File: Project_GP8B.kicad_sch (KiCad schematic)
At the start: 19 parts

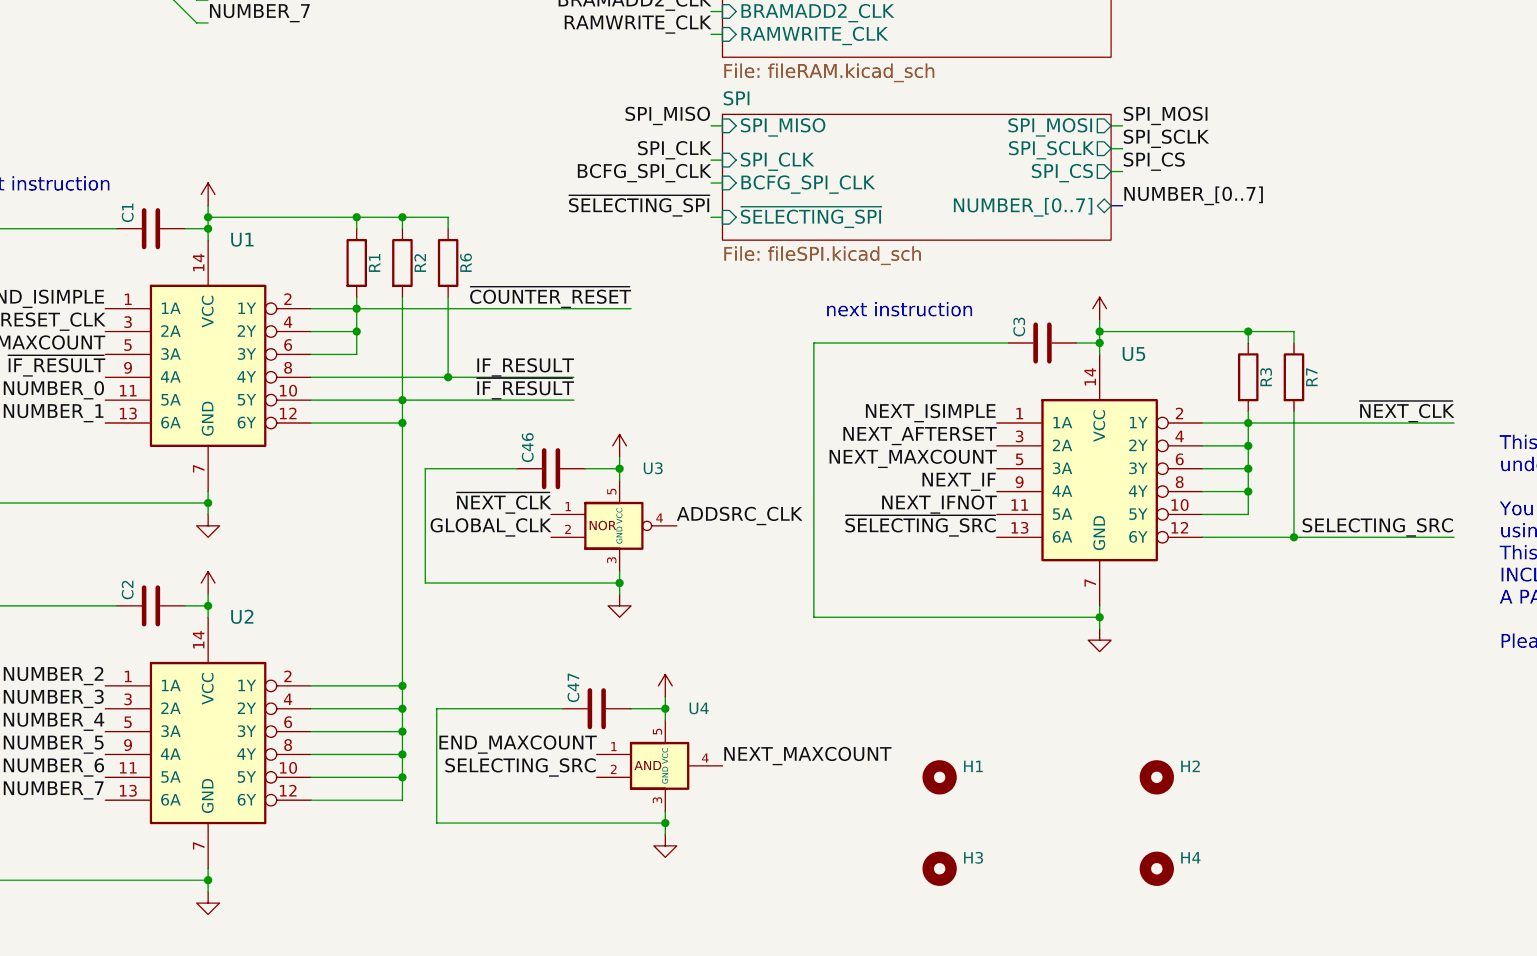
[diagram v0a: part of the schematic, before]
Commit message: Updating descriptions
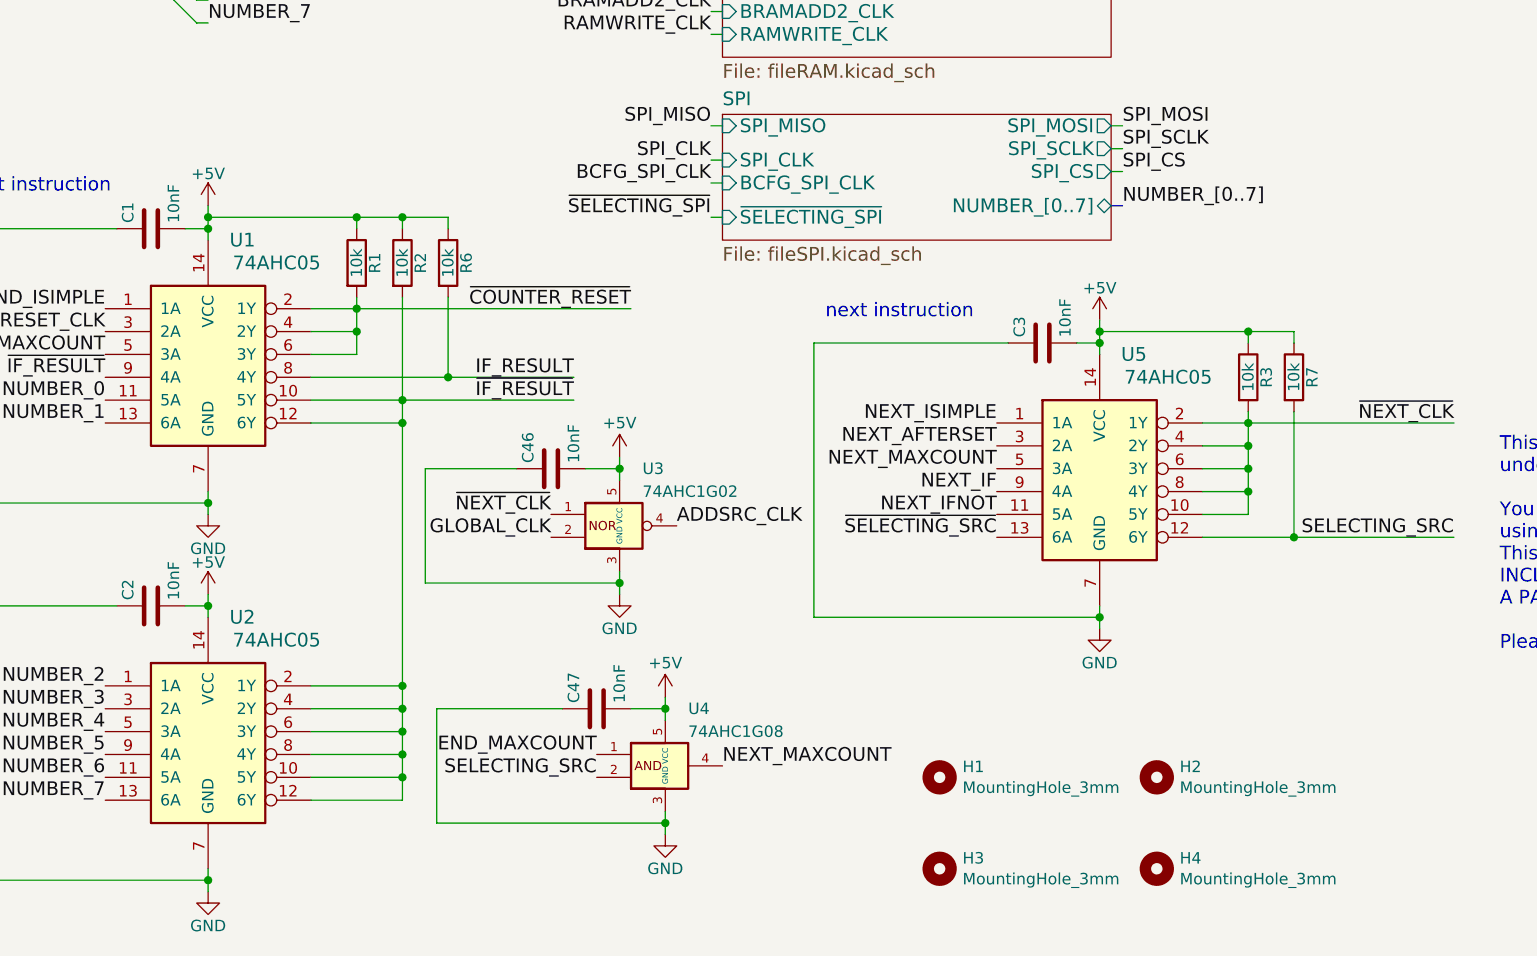
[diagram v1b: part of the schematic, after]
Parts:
- C1, C2, C3, C46, C47: value (none) -> 10nF; footprint (none) -> Capacitor_SMD:C_0805_2012Metric
- H1, H2, H3, H4: value (none) -> MountingHole_3mm; footprint (none) -> MountingHole:MountingHole_3mm
- R1, R2, R3, R6, R7: value (none) -> 10k; footprint (none) -> Resistor_SMD:R_0805_2012Metric
- U1, U2, U5: value (none) -> 74AHC05; footprint (none) -> Package_SO:SOIC-14_3.9x8.7mm_P1.27mm
- U3: value (none) -> 74AHC1G02; footprint (none) -> Package_TO_SOT_SMD:SOT-23-5
- U4: value (none) -> 74AHC1G08; footprint (none) -> Package_TO_SOT_SMD:SOT-23-5

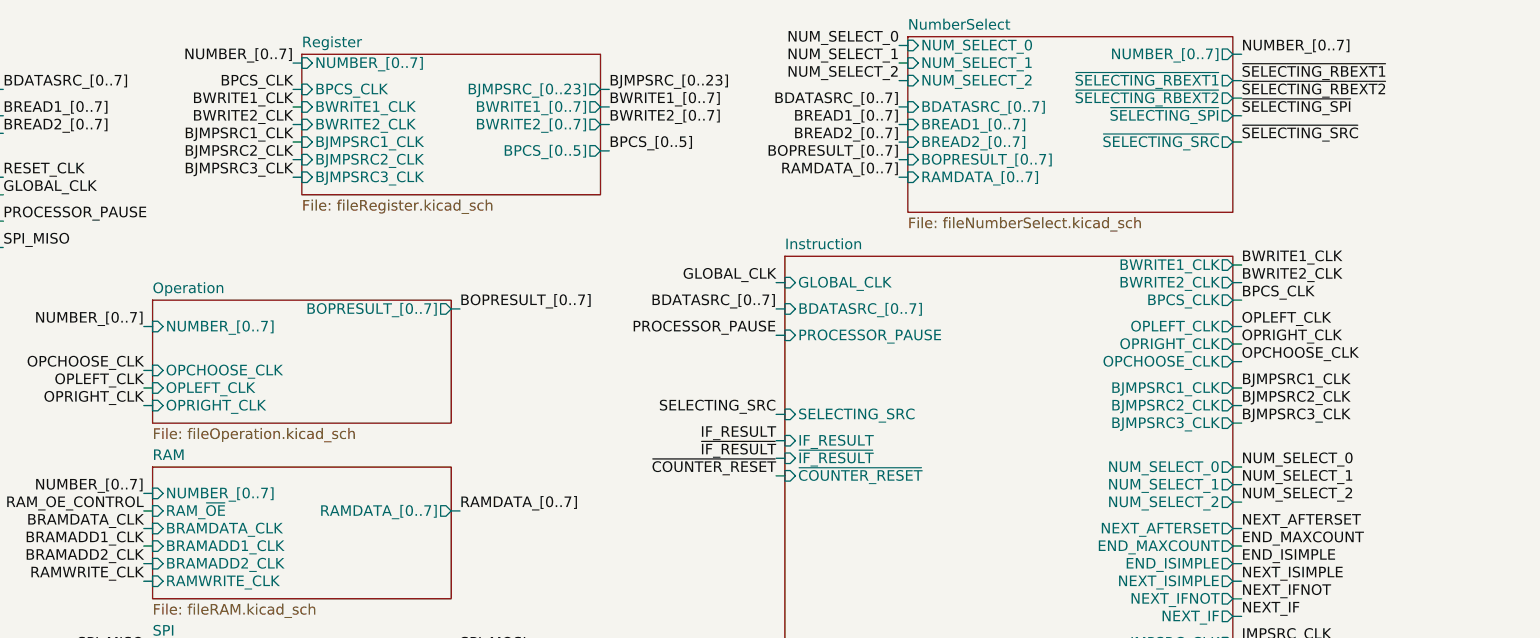
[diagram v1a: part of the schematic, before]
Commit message: Renaming COUNTER to SEQUENCE and others to make it clear
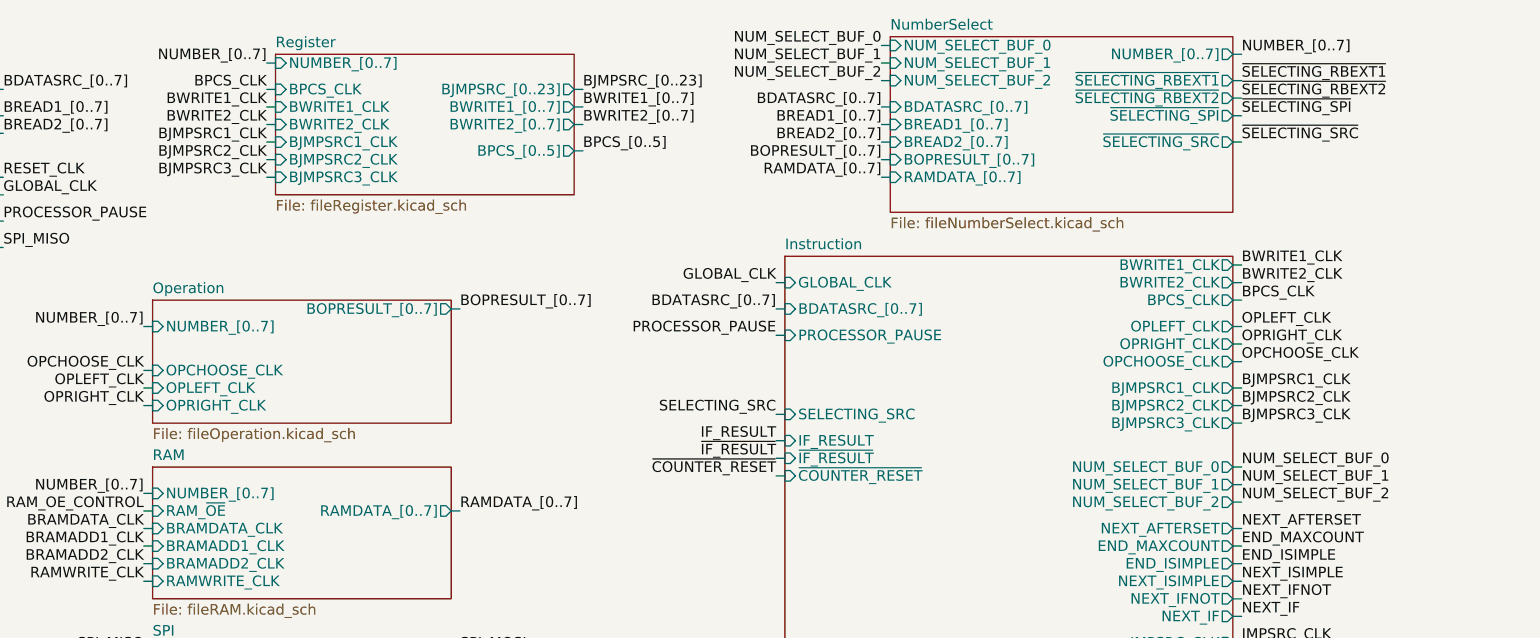
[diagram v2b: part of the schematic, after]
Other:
- sheet Instruction ports: added NUM_SELECT_BUF_0, NUM_SELECT_BUF_1, NUM_SELECT_BUF_2; removed NUM_SELECT_0, NUM_SELECT_1, NUM_SELECT_2
- sheet NumberSelect ports: added NUM_SELECT_BUF_0, NUM_SELECT_BUF_1, NUM_SELECT_BUF_2; removed NUM_SELECT_0, NUM_SELECT_1, NUM_SELECT_2

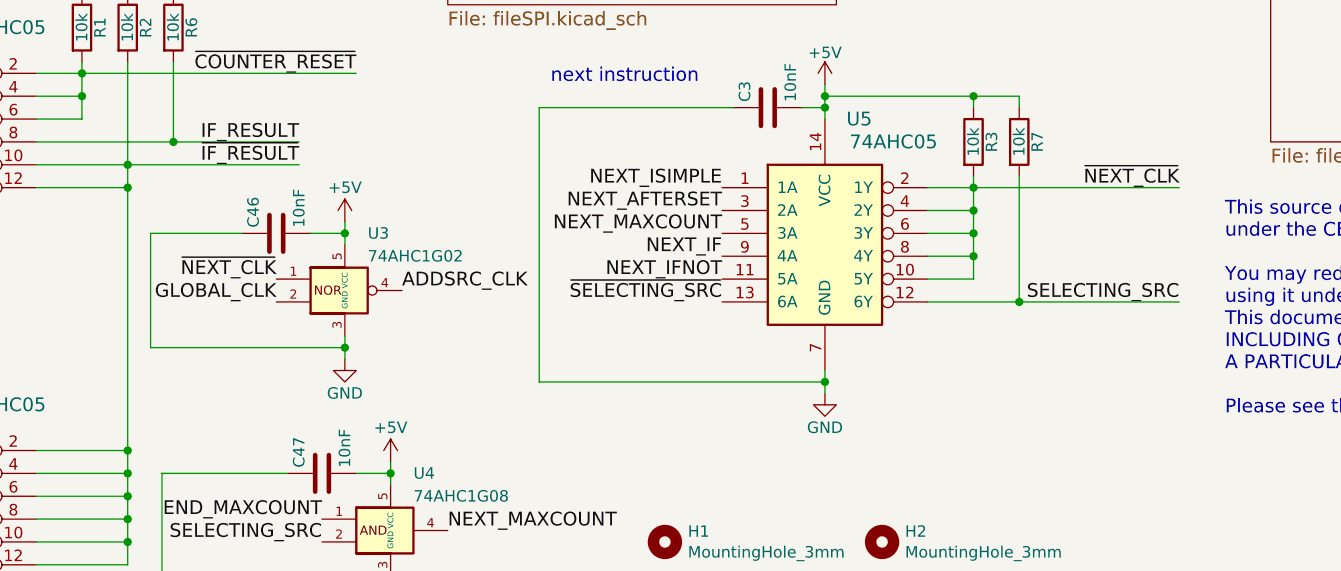
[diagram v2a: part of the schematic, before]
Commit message: Add more sequences to prepare 50MHz compatibility (removing clock sync)
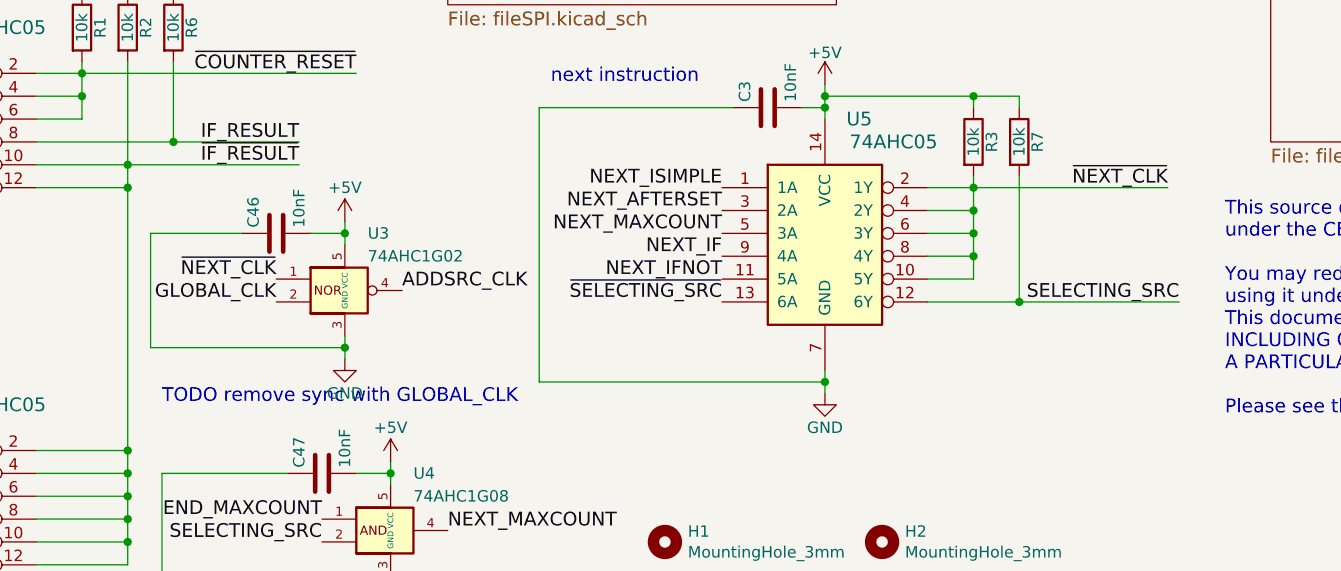
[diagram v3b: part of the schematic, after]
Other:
- note added: "TODO remove sync with GLOBAL_CLK"
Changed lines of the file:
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@@
     (stroke (width 0) (type default) (color 0 0 0 0))
   )
-  (wire (pts (xy 162.56 138.43) (xy 185.42 138.43))
+  (wire (pts (xy 162.56 138.43) (xy 184.15 138.43))
     (stroke (width 0) (type default) (color 0 0 0 0))
   )
@@
   )
   (text "next instruction" (at 115.57 127 0)
+    (effects (font (size 1.524 1.524)) (justify left bottom))
+  )
+  (text "TODO remove sync with GLOBAL_CLK" (at 72.39 162.56 0)
     (effects (font (size 1.524 1.524)) (justify left bottom))
   )
@@
     (effects (font (size 1.524 1.524)) (justify left bottom))
   )
-  (label "~{NEXT_CLK}" (at 185.42 138.43 180)
-    (effects (font (size 1.524 1.524)) (justify right bottom))
-  )
+  (label "~{NEXT_CLK}" (at 184.15 138.43 180)
+    (effects (font (size 1.524 1.524)) (justify right bottom))
+  )

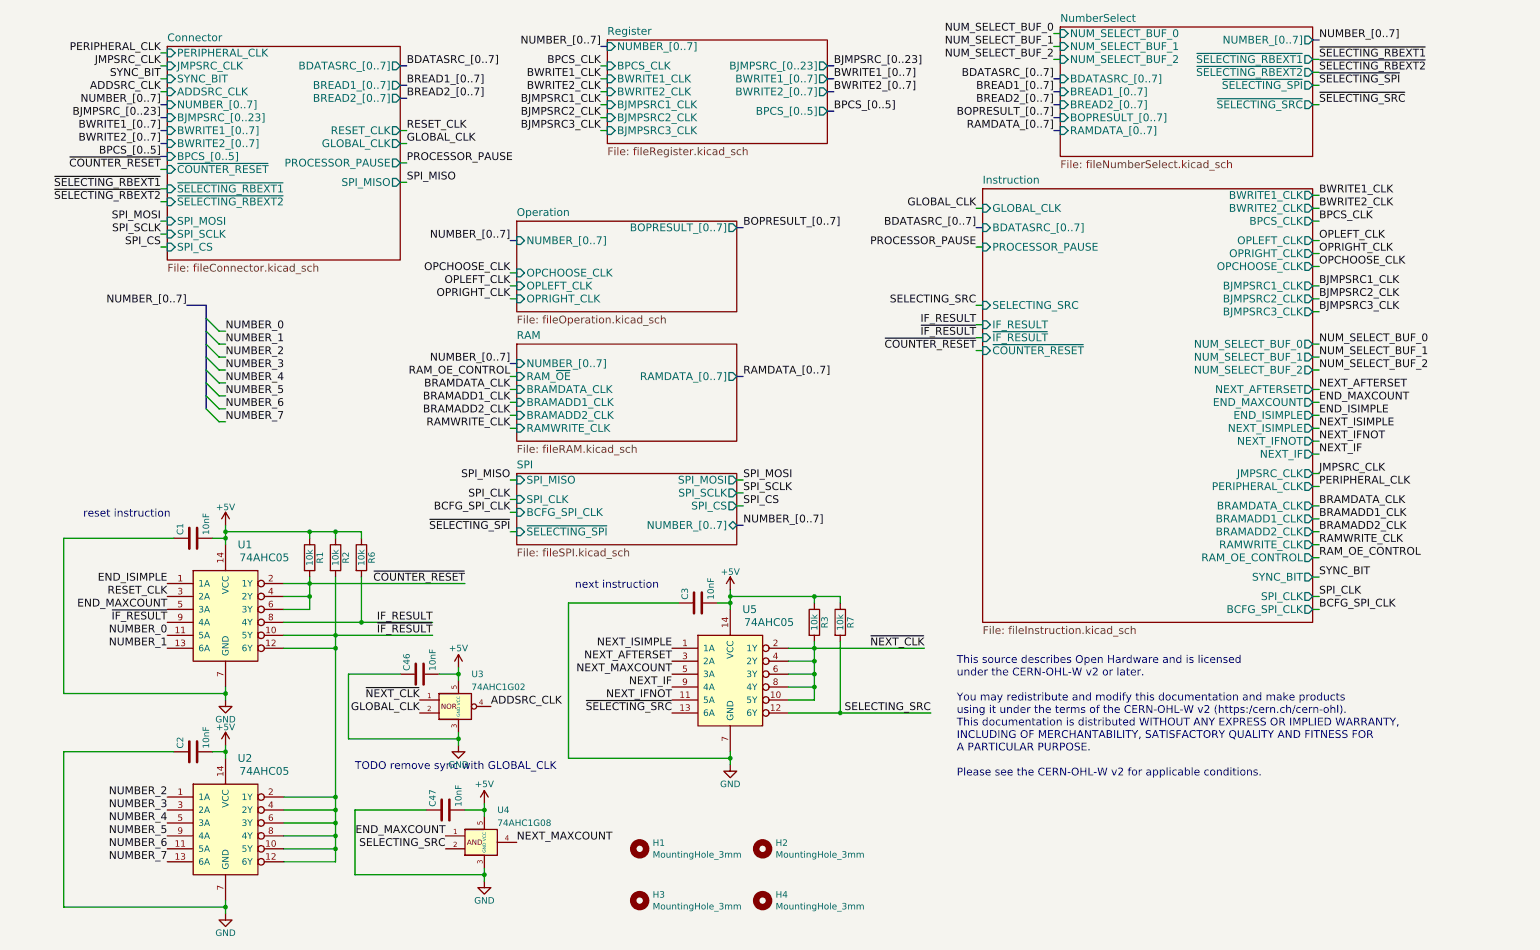
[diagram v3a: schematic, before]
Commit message: Finally remove clock sync, big improvement for the "if" instruction check (faster tps, less gates)
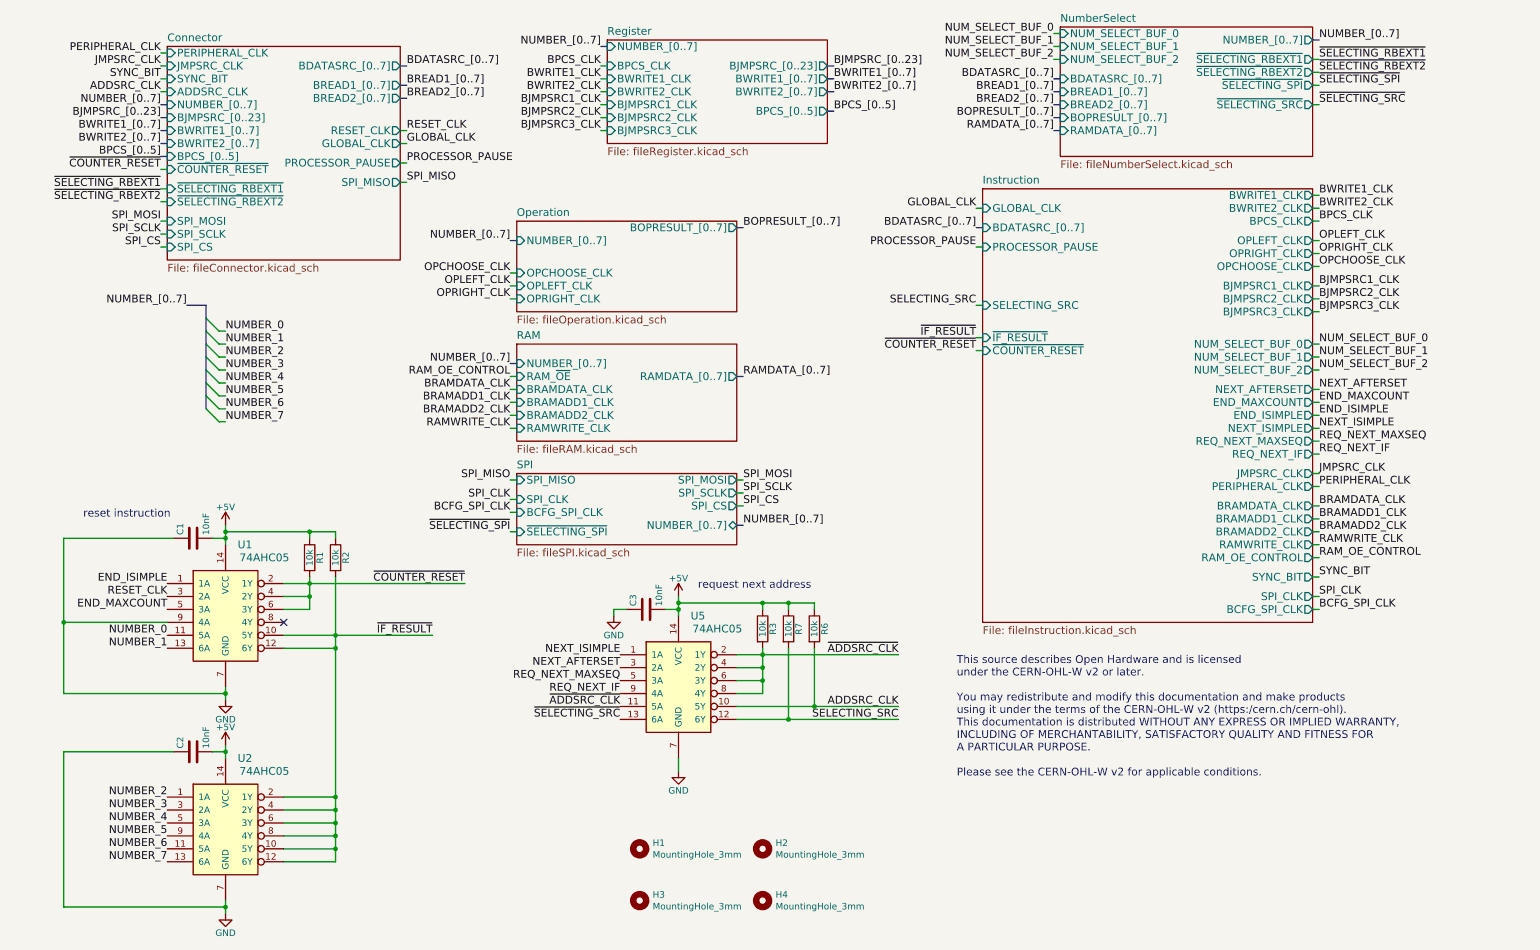
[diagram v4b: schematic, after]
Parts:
- removed C46, C47: 10nF, Capacitor_SMD:C_0805_2012Metric, symbol Device:C
- removed U3: 74AHC1G02, Package_TO_SOT_SMD:SOT-23-5, symbol Custom:74AHC1G02
- removed U4: 74AHC1G08, Package_TO_SOT_SMD:SOT-23-5, symbol Custom:74AHC1G08
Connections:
- net ADDSRC_CLK: now also R6.2, U5.10 (5Y)
- net GND: now also U1.9 (4A)
- net ~{IF_RESULT}: no longer U1.9 (4A)
- net IF_RESULT: no longer names the net of U1.8 (4Y)
- net IF_RESULT: no longer R6.2
- net NEXT_IF renamed REQ_NEXT_IF
- net NEXT_IFNOT renamed ~{ADDSRC_CLK}
- net ~{ADDSRC_CLK}: now also R3.2, U5.2 (1Y), U5.4 (2Y), U5.6 (3Y), U5.8 (4Y)
- net NEXT_MAXCOUNT renamed REQ_NEXT_MAXSEQ
- removed net ~{NEXT_CLK}: R3.2, U5.10 (5Y), U5.2 (1Y), U5.4 (2Y), U5.6 (3Y), U5.8 (4Y)
- no-connect marks 0 -> 1
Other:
- sheet Instruction ports: added REQ_NEXT_IF, REQ_NEXT_MAXSEQ; removed IF_RESULT, NEXT_IF, NEXT_IFNOT
- note added: "request next address"
- note removed: "TODO remove sync with GLOBAL_CLK"
- note removed: "next instruction"
- moved on the sheet: C3, R3, R6, R7, U5

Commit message: bit of cleaning after last commit
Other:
- moved on the sheet: C3, R3, R6, R7, U5
